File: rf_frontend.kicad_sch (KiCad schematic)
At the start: 11 parts, among them U301 BGS12SN6E6327XTSA1, U302 BALFHB-WL-05D3

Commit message: STM power mostly done
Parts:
- added C308: 1n, Capacitor_SMD:C_0402_1005Metric, symbol Device:C
- added C309: 100n, Capacitor_SMD:C_0402_1005Metric, symbol Device:C
- added R302: 100, Resistor_SMD:R_0402_1005Metric, symbol Device:R
- C304, C305: footprint (none) -> Capacitor_SMD:C_0402_1005Metric
- R301: footprint (none) -> Resistor_SMD:R_0402_1005Metric
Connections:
- net GND: now also C308.2, C309.2
- net at U301.4 (VDD): now also C308.1, C309.1, R302.2
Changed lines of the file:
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@@
   (junction (at 109.22 119.38) (diameter 0) (color 0 0 0 0)
   )
+  (junction (at 187.96 72.39) (diameter 0) (color 0 0 0 0)
+  )
   (junction (at 43.18 81.28) (diameter 0) (color 0 0 0 0)
   )
+  (junction (at 176.53 72.39) (diameter 0) (color 0 0 0 0)
+  )
   (junction (at 154.94 137.16) (diameter 0) (color 0 0 0 0)
   )
@@
     (stroke (width 0) (type default))
   )
+  (wire (pts (xy 171.45 72.39) (xy 176.53 72.39))
+    (stroke (width 0) (type default))
+  )
   (wire (pts (xy 54.61 81.28) (xy 66.04 81.28))
     (stroke (width 0) (type default))
@@
     (stroke (width 0) (type default))
   )
+  (wire (pts (xy 198.12 96.52) (xy 194.31 96.52))
+    (stroke (width 0) (type default))
+  )
   (wire (pts (xy 137.16 101.6) (xy 140.97 101.6))
     (stroke (width 0) (type default))
   )
+  (wire (pts (xy 176.53 72.39) (xy 187.96 72.39))
+    (stroke (width 0) (type default))
+  )
   (wire (pts (xy 109.22 119.38) (xy 111.76 119.38))
     (stroke (width 0) (type default))
@@
   )
   (wire (pts (xy 38.1 99.06) (xy 66.04 99.06))
+    (stroke (width 0) (type default))
+  )
+  (wire (pts (xy 187.96 72.39) (xy 198.12 72.39))
+    (stroke (width 0) (type default))
+  )
+  (wire (pts (xy 198.12 72.39) (xy 198.12 96.52))
     (stroke (width 0) (type default))
   )
@@
     (effects (font (size 1.27 1.27)) (justify left bottom))
   )
+  (hierarchical_label "RF_ANT" (shape bidirectional) (at 229.87 101.6 0) (fields_autoplaced)
+    (effects (font (size 1.27 1.27)) (justify left))
+  )
   (hierarchical_label "RF_CTRL" (shape input) (at 137.16 137.16 180) (fields_autoplaced)
     (effects (font (size 1.27 1.27)) (justify right))
@@
   (hierarchical_label "VR_PA" (shape input) (at 38.1 81.28 180) (fields_autoplaced)
     (effects (font (size 1.27 1.27)) (justify right))
+  )
+  (symbol (lib_id "power:GND") (at 176.53 80.01 0) (unit 1)
+    (in_bom yes) (on_board yes) (dnp no) (fields_autoplaced)
+    (property "Reference" "#PWR0308" (at 176.53 86.36 0)
+      (effects (font (size 1.27 1.27)) hide)
+    )
+    (property "Value" "GND" (at 176.53 84.1431 0)
+      (effects (font (size 1.27 1.27)))
+    )
+    (property "Footprint" "" (at 176.53 80.01 0)
+      (effects (font (size 1.27 1.27)) hide)
+    )
+    (property "Datasheet" "" (at 176.53 80.01 0)
+      (effects (font (size 1.27 1.27)) hide)
+    )
+    (pin "1")
+    (instances
+      (project "lora-module"
+        (path "/30c7e509-35af-4828-996b-9681d057624f/8ccb3257-dd21-406f-b73b-aadedfaf4fa0"
+          (reference "#PWR0308") (unit 1)
+        )
+      )
+    )
+  )
+  (symbol (lib_id "Device:R") (at 167.64 72.39 90) (unit 1)
+    (in_bom yes) (on_board yes) (dnp no) (fields_autoplaced)
+    (property "Reference" "R302" (at 167.64 67.2297 90)
+      (effects (font (size 1.27 1.27)))
+    )
+    (property "Value" "100" (at 167.64 69.6539 90)
+      (effects (font (size 1.27 1.27)))
+    )
+    (property "Footprint" "Resistor_SMD:R_0402_1005Metric" (at 167.64 74.168 90)
+      (effects (font (size 1.27 1.27)) hide)
+    )
+    (property "Datasheet" "~" (at 167.64 72.39 0)
+      (effects (font (size 1.27 1.27)) hide)
+    )
+    (pin "1")
+    (pin "2")
+    (instances
+      (project "lora-module"
+        (path "/30c7e509-35af-4828-996b-9681d057624f/8ccb3257-dd21-406f-b73b-aadedfaf4fa0"
+          (reference "R302") (unit 1)
+        )
+      )
+    )
   )
   (symbol (lib_id "power:GND") (at 109.22 119.38 0) (unit 1)
@@
       (effects (font (size 1.27 1.27)) (justify left))
     )
-    (property "Footprint" "" (at 155.9052 144.78 0)
+    (property "Footprint" "Capacitor_SMD:C_0402_1005Metric" (at 155.9052 144.78 0)
       (effects (font (size 1.27 1.27)) hide)
     )
@@
     )
   )
+  (symbol (lib_id "Device:C") (at 176.53 76.2 0) (unit 1)
+    (in_bom yes) (on_board yes) (dnp no) (fields_autoplaced)
+    (property "Reference" "C308" (at 179.451 74.9879 0)
+      (effects (font (size 1.27 1.27)) (justify left))
+    )
+    (property "Value" "1n" (at 179.451 77.4121 0)
+      (effects (font (size 1.27 1.27)) (justify left))
+    )
+    (property "Footprint" "Capacitor_SMD:C_0402_1005Metric" (at 177.4952 80.01 0)
+      (effects (font (size 1.27 1.27)) hide)
+    )
+    (property "Datasheet" "~" (at 176.53 76.2 0)
+      (effects (font (size 1.27 1.27)) hide)
+    )
+    (pin "1")
+    (pin "2")
+    (instances
+      (project "lora-module"
+        (path "/30c7e509-35af-4828-996b-9681d057624f/8ccb3257-dd21-406f-b73b-aadedfaf4fa0"
+          (reference "C308") (unit 1)
+        )
+      )
+    )
+  )
   (symbol (lib_id "Device:C") (at 153.67 99.06 90) (unit 1)
     (in_bom yes) (on_board yes) (dnp no)
@@
         (path "/30c7e509-35af-4828-996b-9681d057624f/8ccb3257-dd21-406f-b73b-aadedfaf4fa0"
           (reference "C306") (unit 1)
+        )
+      )
+    )
+  )
+  (symbol (lib_id "Device:C") (at 187.96 76.2 0) (unit 1)
+    (in_bom yes) (on_board yes) (dnp no) (fields_autoplaced)
+    (property "Reference" "C309" (at 190.881 74.9879 0)
+      (effects (font (size 1.27 1.27)) (justify left))
+    )
+    (property "Value" "100n" (at 190.881 77.4121 0)
+      (effects (font (size 1.27 1.27)) (justify left))
+    )
+    (property "Footprint" "Capacitor_SMD:C_0402_1005Metric" (at 188.9252 80.01 0)
+      (effects (font (size 1.27 1.27)) hide)
+    )
+    (property "Datasheet" "~" (at 187.96 76.2 0)
+      (effects (font (size 1.27 1.27)) hide)
+    )
+    (pin "1")
+    (pin "2")
+    (instances
+      (project "lora-module"
+        (path "/30c7e509-35af-4828-996b-9681d057624f/8ccb3257-dd21-406f-b73b-aadedfaf4fa0"
+          (reference "C309") (unit 1)
         )
       )
@@
     )
   )
+  (symbol (lib_id "power:GND") (at 187.96 80.01 0) (unit 1)
+    (in_bom yes) (on_board yes) (dnp no) (fields_autoplaced)
+    (property "Reference" "#PWR0309" (at 187.96 86.36 0)
+      (effects (font (size 1.27 1.27)) hide)
+    )
+    (property "Value" "GND" (at 187.96 84.1431 0)
+      (effects (font (size 1.27 1.27)))
+    )
+    (property "Footprint" "" (at 187.96 80.01 0)
+      (effects (font (size 1.27 1.27)) hide)
+    )
+    (property "Datasheet" "" (at 187.96 80.01 0)
+      (effects (font (size 1.27 1.27)) hide)
+    )
+    (pin "1")
+    (instances
+      (project "lora-module"
+        (path "/30c7e509-35af-4828-996b-9681d057624f/8ccb3257-dd21-406f-b73b-aadedfaf4fa0"
+          (reference "#PWR0309") (unit 1)
+        )
+      )
+    )
+  )
   (symbol (lib_id "Device:C") (at 73.66 99.06 90) (unit 1)
     (in_bom yes) (on_board yes) (dnp no)
@@
       (effects (font (size 1.27 1.27)) (justify left))
     )
-    (property "Footprint" "" (at 167.3352 144.78 0)
+    (property "Footprint" "Capacitor_SMD:C_0402_1005Metric" (at 167.3352 144.78 0)
       (effects (font (size 1.27 1.27)) hide)
     )
@@
       (effects (font (size 1.27 1.27)))
     )
-    (property "Footprint" "" (at 146.05 138.938 90)
-      (effects (font (size 1.27 1.27)) hide)
-    )
+    (property "Footprint" "Resistor_SMD:R_0402_1005Metric" (at 146.05 138.938 90)
+      (effects (font (size 1.27 1.27)) hide)
+    )

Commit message: added cubemx file for checking pinout
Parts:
- C301, C303, C306, C307: footprint (none) -> Capacitor_SMD:C_0402_1005Metric
- C302: footprint (none) -> Capacitor_SMD:C_0603_1608Metric
- L301: footprint (none) -> Inductor_SMD:L_0402_1005Metric
- U302: footprint BGA8_BALFHB_STM -> lora-module:BGA8_BALFHB_STM
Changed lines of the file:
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@@
       (effects (font (size 1.27 1.27)) (justify left))
     )
-    (property "Footprint" "" (at 44.1452 88.9 0)
+    (property "Footprint" "Capacitor_SMD:C_0603_1608Metric" (at 44.1452 88.9 0)
       (effects (font (size 1.27 1.27)) hide)
     )
@@
       (effects (font (size 1.27 1.27)) (justify left))
     )
-    (property "Footprint" "" (at 154.6352 113.03 0)
+    (property "Footprint" "Capacitor_SMD:C_0402_1005Metric" (at 154.6352 113.03 0)
       (effects (font (size 1.27 1.27)) hide)
     )
@@
       (effects (font (size 1.27 1.27)) (justify left))
     )
-    (property "Footprint" "" (at 55.5752 88.9 0)
+    (property "Footprint" "Capacitor_SMD:C_0402_1005Metric" (at 55.5752 88.9 0)
       (effects (font (size 1.27 1.27)) hide)
     )
@@
       (effects (font (size 1.27 1.27)))
     )
-    (property "Footprint" "" (at 157.48 98.0948 0)
+    (property "Footprint" "Capacitor_SMD:C_0402_1005Metric" (at 157.48 98.0948 0)
       (effects (font (size 1.27 1.27)) hide)
     )
@@
       (effects (font (size 1.524 1.524)))
     )
-    (property "Footprint" "BGA8_BALFHB_STM" (at 81.28 99.06 0)
+    (property "Footprint" "lora-module:BGA8_BALFHB_STM" (at 81.28 99.06 0)
       (effects (font (size 1.27 1.27) italic) hide)
     )
@@
       (effects (font (size 1.27 1.27)) (justify left))
     )
-    (property "Footprint" "" (at 66.04 85.09 0)
+    (property "Footprint" "Inductor_SMD:L_0402_1005Metric" (at 66.04 85.09 0)
       (effects (font (size 1.27 1.27)) hide)
     )
@@
       (effects (font (size 1.27 1.27)))
     )
-    (property "Footprint" "" (at 77.47 98.0948 0)
-      (effects (font (size 1.27 1.27)) hide)
-    )
+    (property "Footprint" "Capacitor_SMD:C_0402_1005Metric" (at 77.47 98.0948 0)
+      (effects (font (size 1.27 1.27)) hide)
+    )

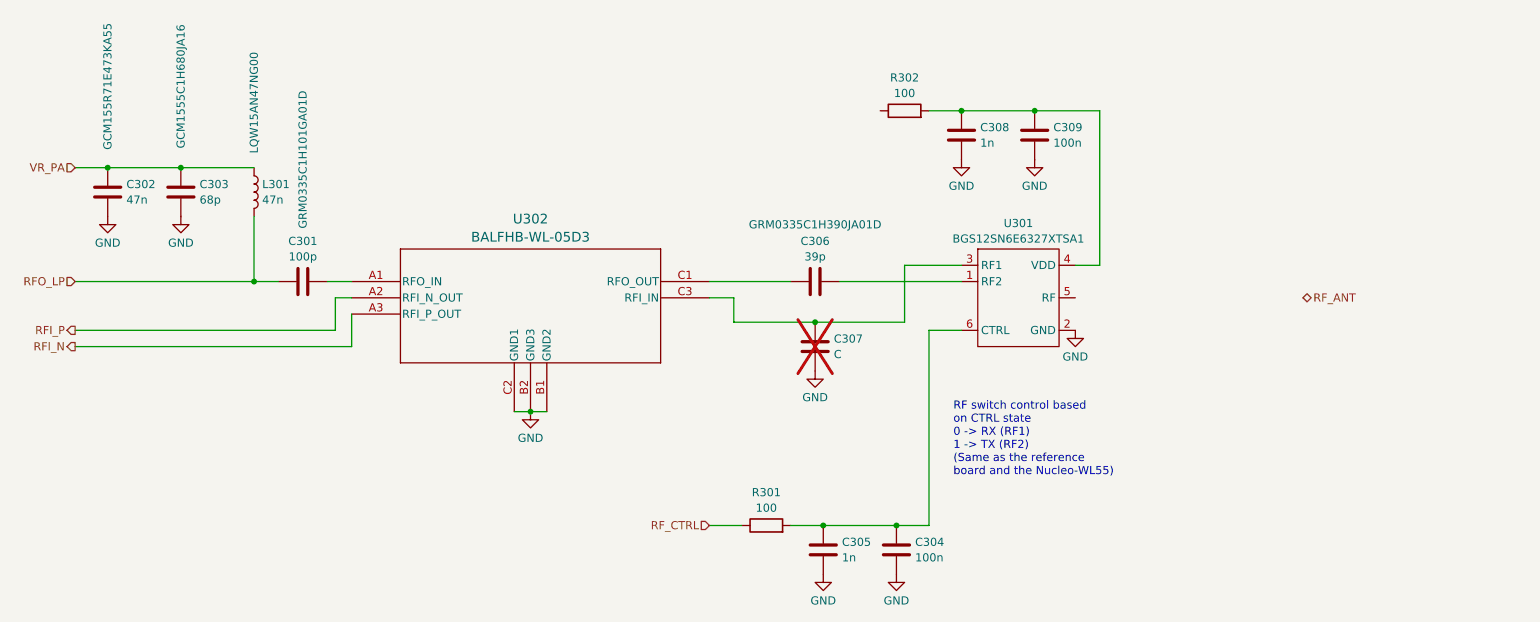
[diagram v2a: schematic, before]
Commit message: most components placed, routed the RF section
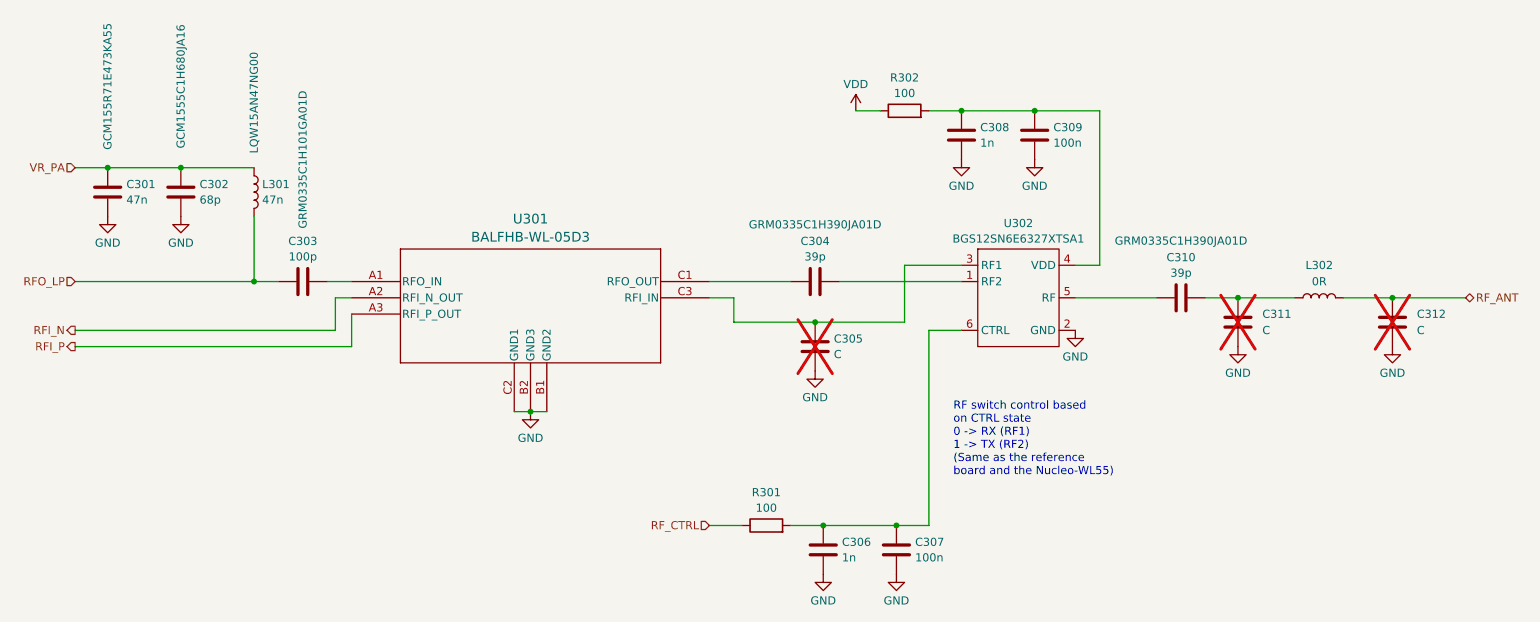
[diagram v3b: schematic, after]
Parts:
- added C310: 39p, Capacitor_SMD:C_0402_1005Metric, symbol Device:C
- added C311, C312: C, Capacitor_SMD:C_0402_1005Metric_Pad0.74x0.62mm_HandSolder, symbol Device:C
- added L302: 0R, Inductor_SMD:L_0402_1005Metric_Pad0.77x0.64mm_HandSolder, symbol Device:L
- C305: renamed from C307; footprint Capacitor_SMD:C_0402_1005Metric -> Capacitor_SMD:C_0402_1005Metric_Pad0.74x0.62mm_HandSolder
- renumbered C302 to C301, C303 to C302, C301 to C303, C306 to C304, C305 to C306, C304 to C307, U302 to U301, U301 to U302
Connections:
- net GND: now also C311.2, C312.2
- net RFI_N: now also U301.A2 (RFI_N_OUT); no longer U301.A3 (RFI_P_OUT)
- net RFI_P: now also U301.A3 (RFI_P_OUT); no longer U301.A2 (RFI_N_OUT)
- net RF_ANT: now also C312.1, L302.2
- net VDD: now reaches R302.1
- net at U302.5 (RF): now also C310.1
- new net: C310.2, C311.1, L302.1

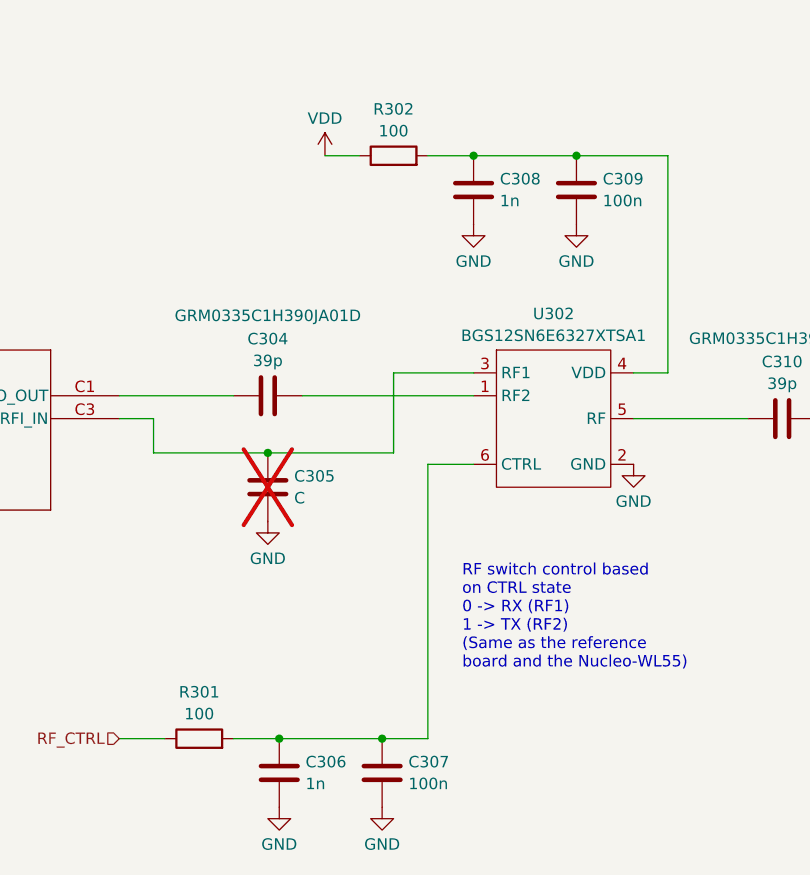
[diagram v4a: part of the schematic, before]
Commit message: added tag-connect and a led, noticed i forgot a crystal
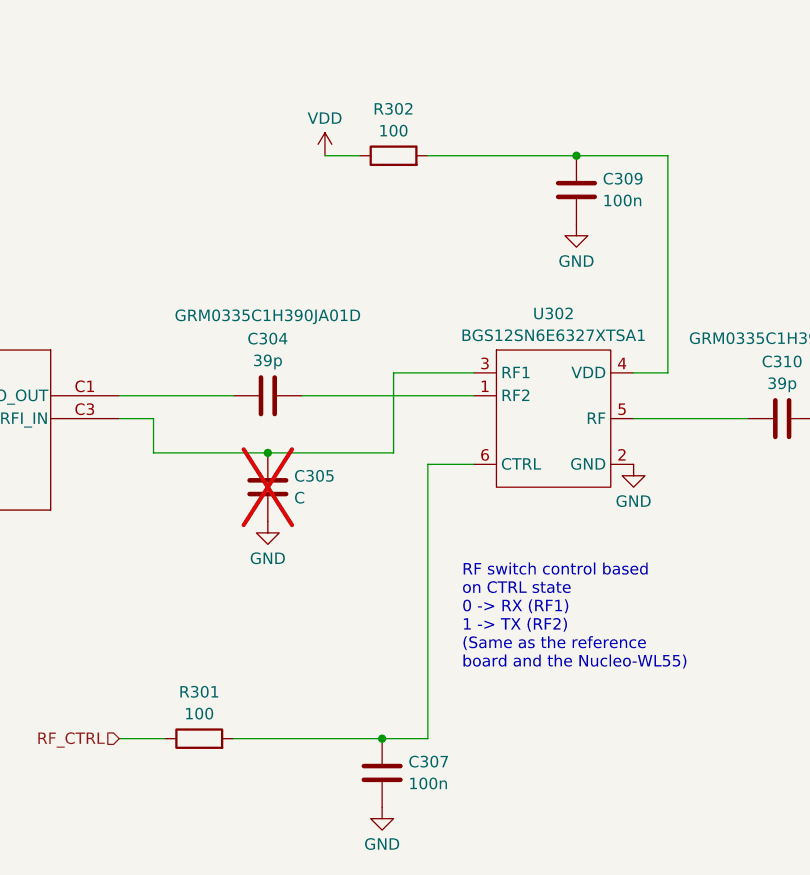
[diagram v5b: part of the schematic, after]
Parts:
- removed C306, C308: 1n, Capacitor_SMD:C_0402_1005Metric, symbol Device:C
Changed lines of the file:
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@@
   (junction (at 243.84 101.6) (diameter 0) (color 0 0 0 0)
   )
-  (junction (at 176.53 72.39) (diameter 0) (color 0 0 0 0)
-  )
-  (junction (at 154.94 137.16) (diameter 0) (color 0 0 0 0)
-  )
   (junction (at 66.04 99.06) (diameter 0) (color 0 0 0 0)
   )
@@
     (stroke (width 0) (type default))
   )
-  (wire (pts (xy 154.94 137.16) (xy 166.37 137.16))
+  (wire (pts (xy 149.86 137.16) (xy 166.37 137.16))
     (stroke (width 0) (type default))
   )
@@
     (stroke (width 0) (type default))
   )
-  (wire (pts (xy 171.45 72.39) (xy 176.53 72.39))
+  (wire (pts (xy 171.45 72.39) (xy 187.96 72.39))
     (stroke (width 0) (type default))
   )
@@
     (stroke (width 0) (type default))
   )
-  (wire (pts (xy 176.53 72.39) (xy 187.96 72.39))
-    (stroke (width 0) (type default))
-  )
   (wire (pts (xy 109.22 119.38) (xy 111.76 119.38))
     (stroke (width 0) (type default))
@@
   )
   (wire (pts (xy 106.68 119.38) (xy 109.22 119.38))
-    (stroke (width 0) (type default))
-  )
-  (wire (pts (xy 149.86 137.16) (xy 154.94 137.16))
     (stroke (width 0) (type default))
   )
@@
     )
   )
-  (symbol (lib_id "power:GND") (at 176.53 80.01 0) (unit 1)
-    (in_bom yes) (on_board yes) (dnp no) (fields_autoplaced)
-    (property "Reference" "#PWR0308" (at 176.53 86.36 0)
-      (effects (font (size 1.27 1.27)) hide)
-    )
-    (property "Value" "GND" (at 176.53 84.1431 0)
-      (effects (font (size 1.27 1.27)))
-    )
-    (property "Footprint" "" (at 176.53 80.01 0)
-      (effects (font (size 1.27 1.27)) hide)
-    )
-    (property "Datasheet" "" (at 176.53 80.01 0)
-      (effects (font (size 1.27 1.27)) hide)
-    )
-    (pin "1")
-    (instances
-      (project "lora-module"
-        (path "/30c7e509-35af-4828-996b-9681d057624f/8ccb3257-dd21-406f-b73b-aadedfaf4fa0"
-          (reference "#PWR0308") (unit 1)
-        )
-      )
-    )
-  )
   (symbol (lib_id "Device:R") (at 167.64 72.39 90) (unit 1)
     (in_bom yes) (on_board yes) (dnp no) (fields_autoplaced)
@@
     )
   )
-  (symbol (lib_id "power:GND") (at 154.94 144.78 0) (unit 1)
-    (in_bom yes) (on_board yes) (dnp no) (fields_autoplaced)
-    (property "Reference" "#PWR0305" (at 154.94 151.13 0)
-      (effects (font (size 1.27 1.27)) hide)
-    )
-    (property "Value" "GND" (at 154.94 148.9131 0)
-      (effects (font (size 1.27 1.27)))
-    )
-    (property "Footprint" "" (at 154.94 144.78 0)
-      (effects (font (size 1.27 1.27)) hide)
-    )
-    (property "Datasheet" "" (at 154.94 144.78 0)
-      (effects (font (size 1.27 1.27)) hide)
-    )
-    (pin "1")
-    (instances
-      (project "lora-module"
-        (path "/30c7e509-35af-4828-996b-9681d057624f/8ccb3257-dd21-406f-b73b-aadedfaf4fa0"
-          (reference "#PWR0305") (unit 1)
-        )
-      )
-    )
-  )
-  (symbol (lib_id "Device:C") (at 154.94 140.97 0) (unit 1)
-    (in_bom yes) (on_board yes) (dnp no) (fields_autoplaced)
-    (property "Reference" "C306" (at 157.861 139.7579 0)
-      (effects (font (size 1.27 1.27)) (justify left))
-    )
-    (property "Value" "1n" (at 157.861 142.1821 0)
-      (effects (font (size 1.27 1.27)) (justify left))
-    )
-    (property "Footprint" "Capacitor_SMD:C_0402_1005Metric" (at 155.9052 144.78 0)
-      (effects (font (size 1.27 1.27)) hide)
-    )
-    (property "Datasheet" "~" (at 154.94 140.97 0)
-      (effects (font (size 1.27 1.27)) hide)
-    )
-    (pin "1")
-    (pin "2")
-    (instances
-      (project "lora-module"
-        (path "/30c7e509-35af-4828-996b-9681d057624f/8ccb3257-dd21-406f-b73b-aadedfaf4fa0"
-          (reference "C306") (unit 1)
-        )
-      )
-    )
-  )
   (symbol (lib_id "power:VDD") (at 160.02 72.39 0) (unit 1)
     (in_bom yes) (on_board yes) (dnp no) (fields_autoplaced)
@@
         )
       )
-    )
-  )
-  (symbol (lib_id "Device:C") (at 176.53 76.2 0) (unit 1)
-    (in_bom yes) (on_board yes) (dnp no) (fields_autoplaced)
-    (property "Reference" "C308" (at 179.451 74.9879 0)
-      (effects (font (size 1.27 1.27)) (justify left))
-    )
-    (property "Value" "1n" (at 179.451 77.4121 0)
-      (effects (font (size 1.27 1.27)) (justify left))
-    )
-    (property "Footprint" "Capacitor_SMD:C_0402_1005Metric" (at 177.4952 80.01 0)
-      (effects (font (size 1.27 1.27)) hide)
-    )
-    (property "Datasheet" "~" (at 176.53 76.2 0)
-      (effects (font (size 1.27 1.27)) hide)
-    )
-    (pin "1")
-    (pin "2")
-    (instances
-      (project "lora-module"
-        (path "/30c7e509-35af-4828-996b-9681d057624f/8ccb3257-dd21-406f-b73b-aadedfaf4fa0"
-          (reference "C308") (unit 1)
-        )
-      )
